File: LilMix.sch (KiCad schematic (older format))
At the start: 60 parts, among them J1_L1 MONO, J1_R1 MONO, J2_L1 MONO, J2_R1 MONO, J3 STEREO, J4 MONO, J5 MONO, J6 STEREO, U1 TL074, U2 NE5532

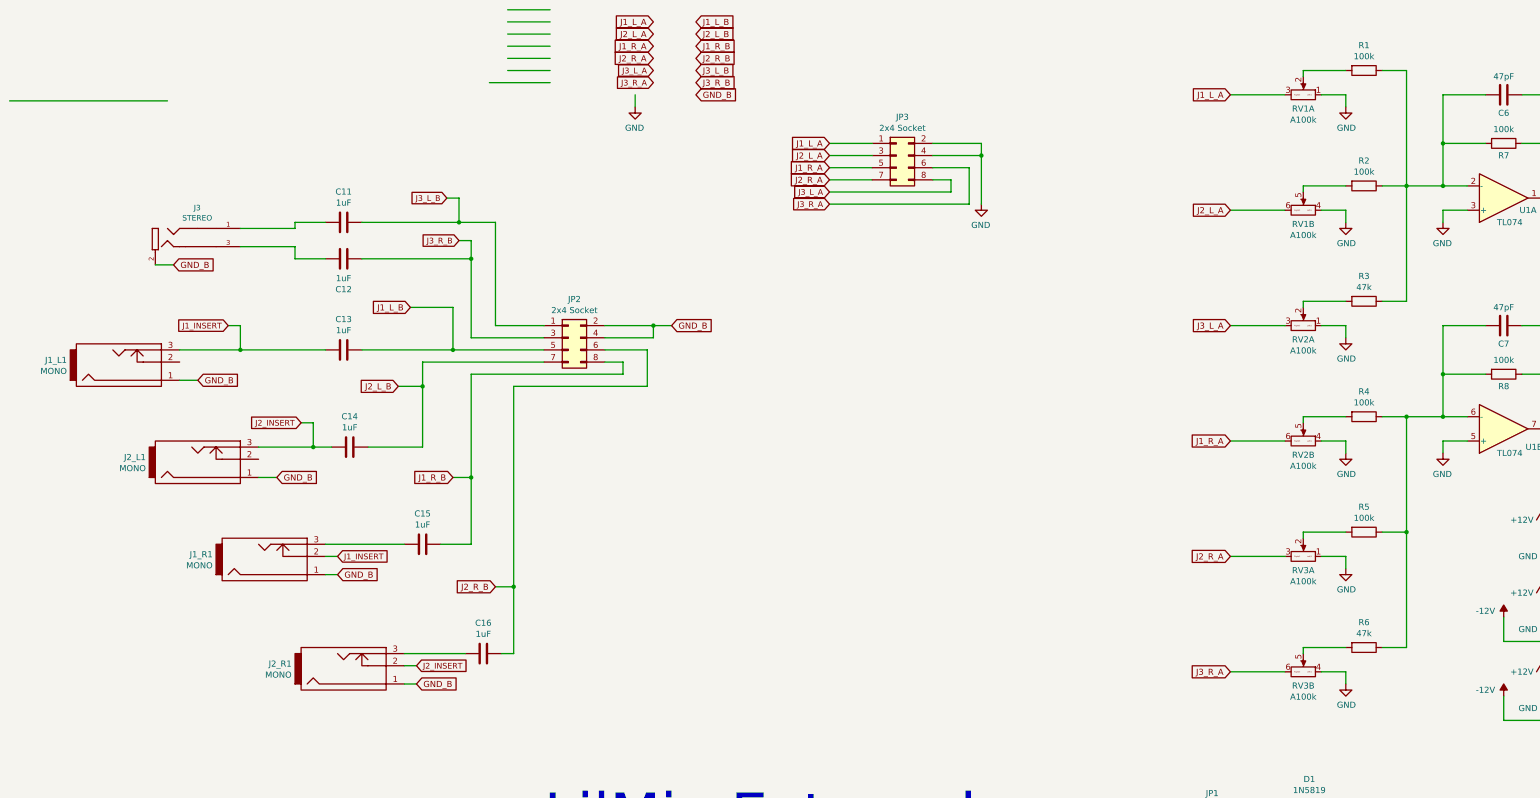
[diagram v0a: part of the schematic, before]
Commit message: Fixed jack destinatios and flipped front board orientation. Rerouted pcb
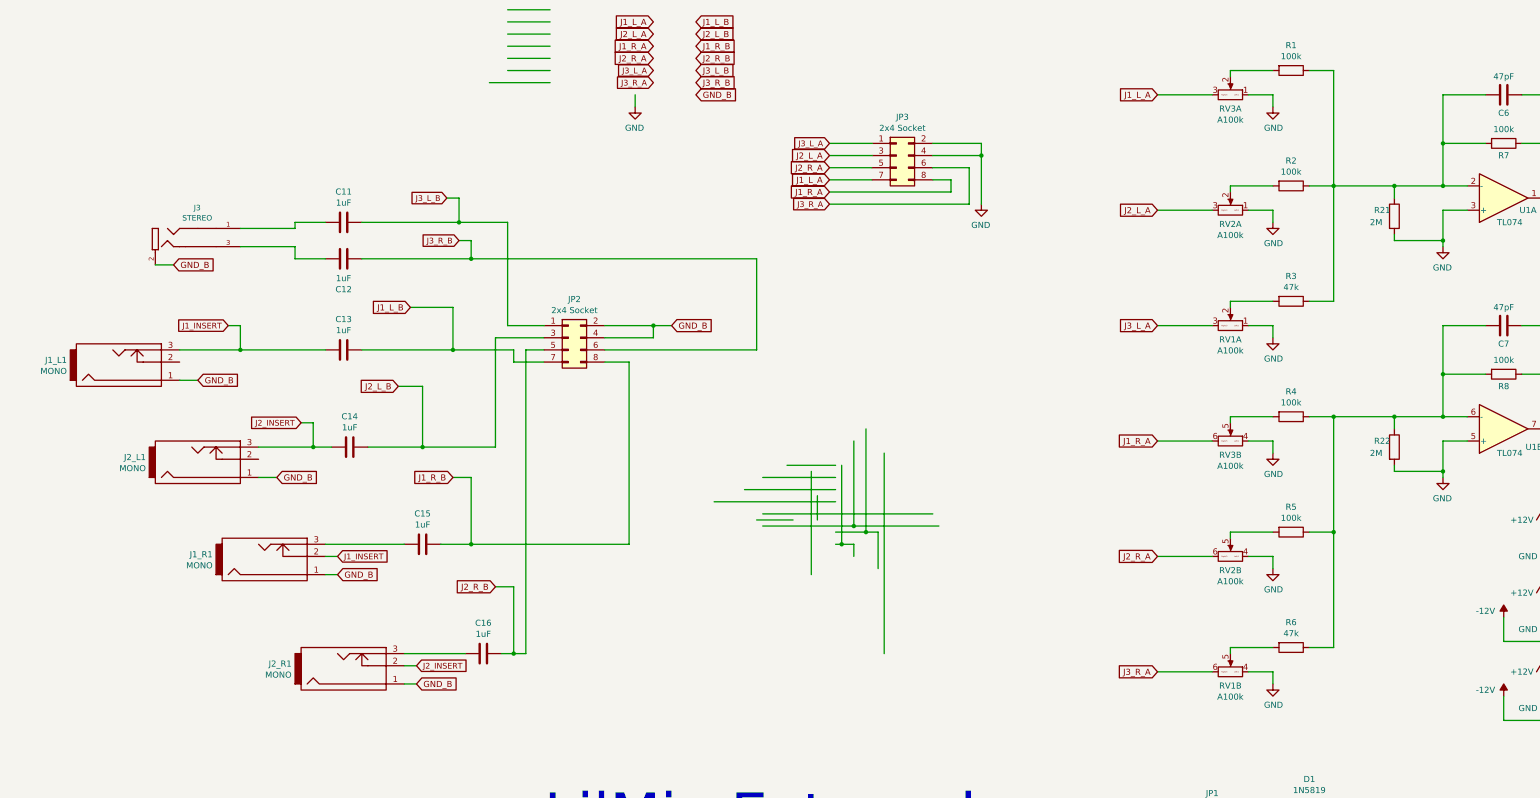
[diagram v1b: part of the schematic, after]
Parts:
- added R21, R22: 2M, Resistor_SMD:R_0805_2012Metric_Pad1.15x1.40mm_HandSolder, symbol 4ms-passives:R
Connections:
- wire segments 291 -> 322
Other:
- moved on the sheet: R1, R2, R3, R4, R5, R6, RV1A, RV1B, RV2A, RV2B, RV3A, RV3B

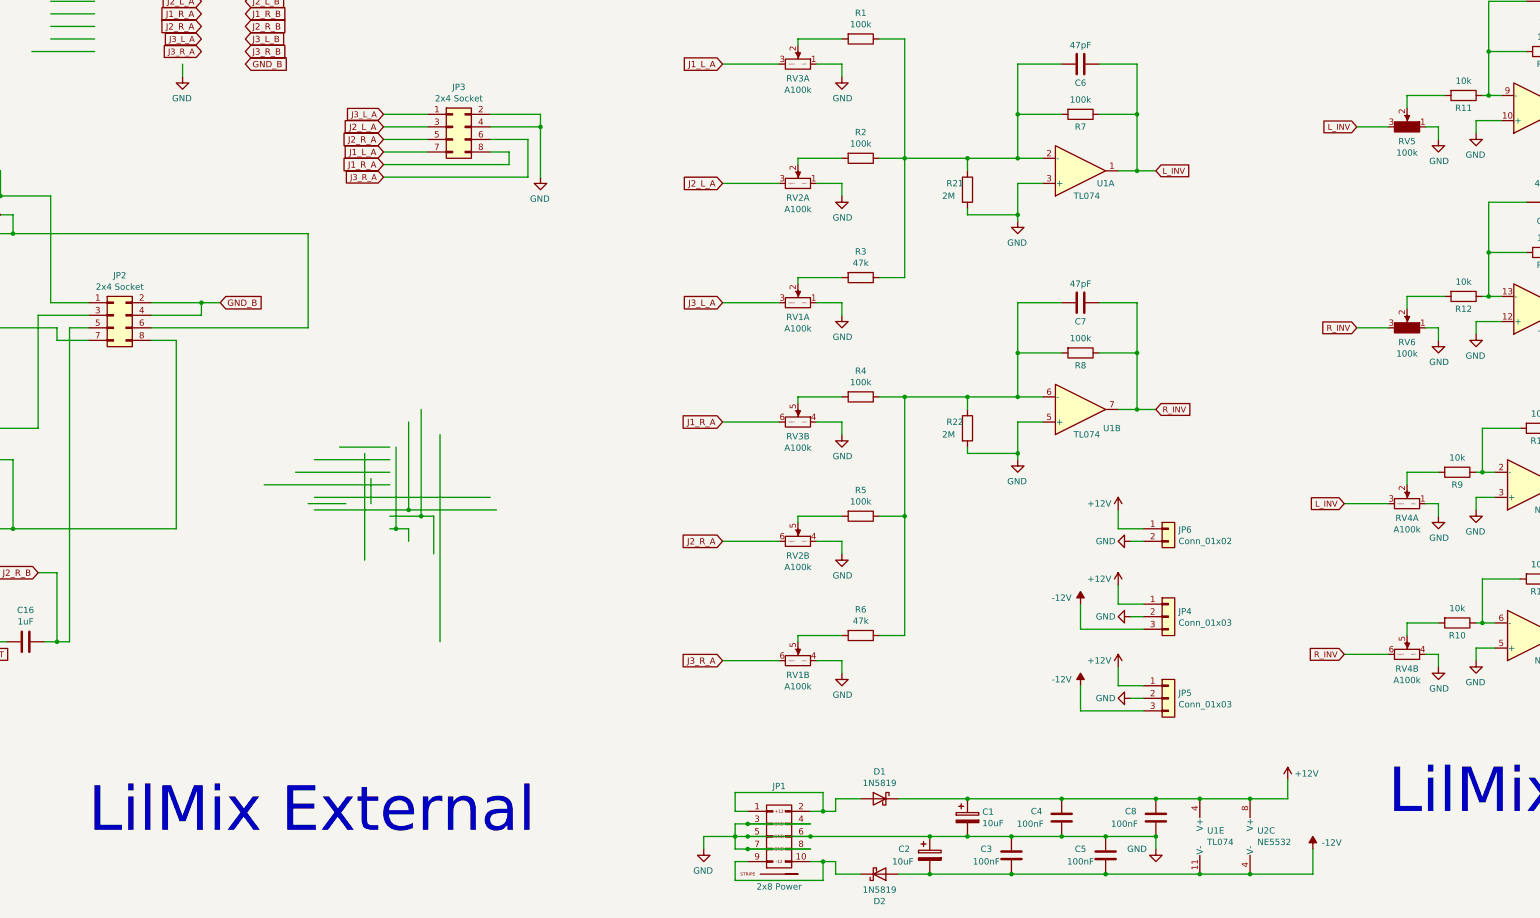
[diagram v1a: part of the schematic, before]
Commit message: Components moved, board wiring needs to be redone. Removed trim pots on line out. Replaced jacks on large board
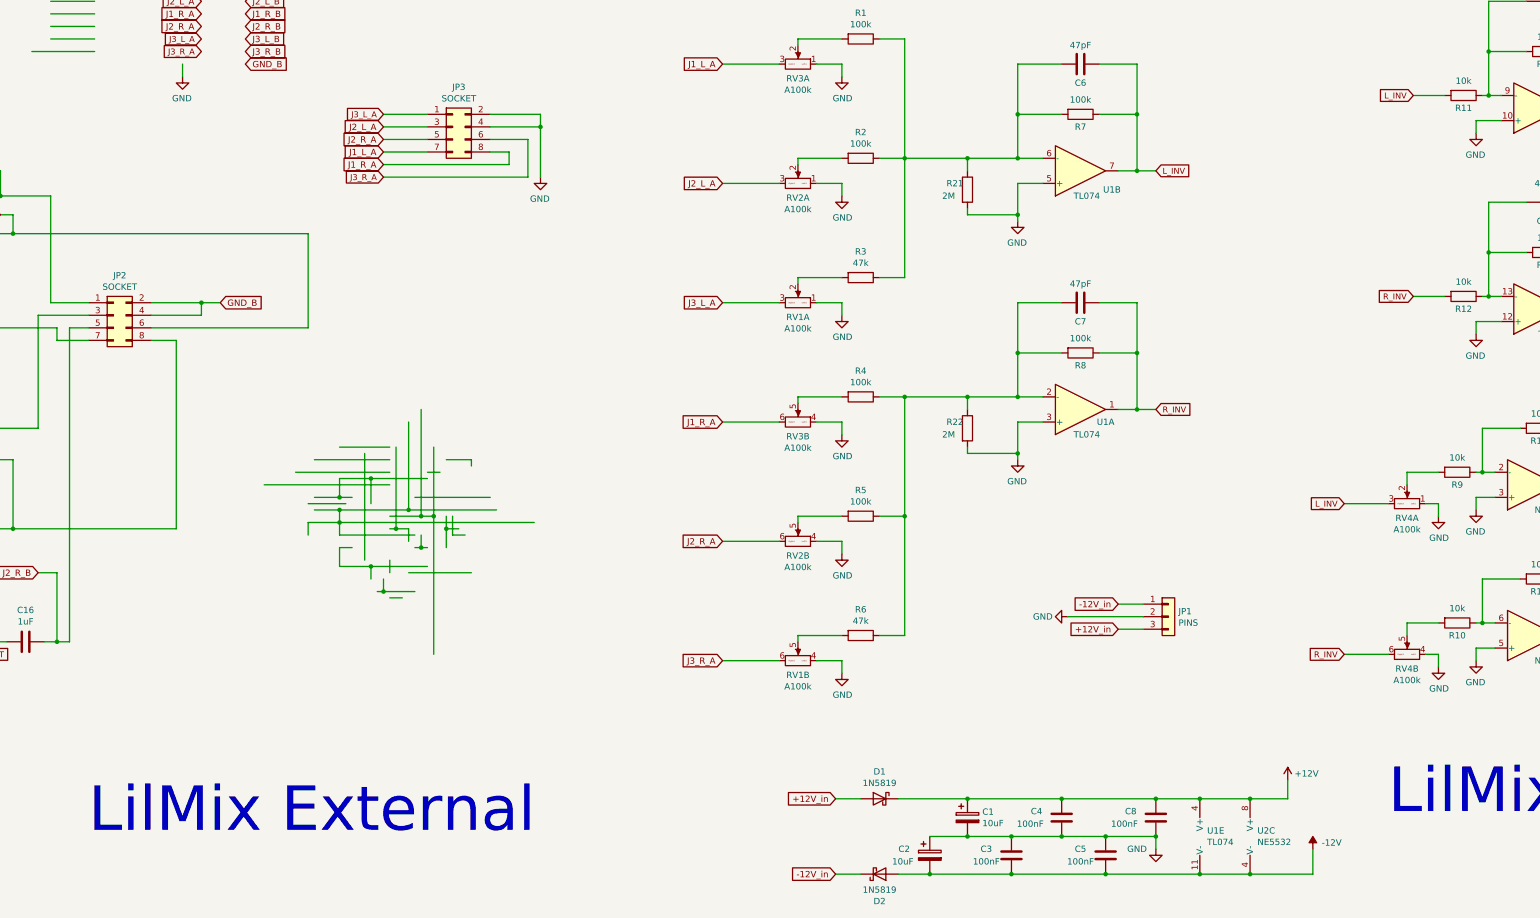
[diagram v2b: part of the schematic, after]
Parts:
- removed JP1: 2x8 Power, 4ms-footprints:Header_2x05_Pitch2.54mm_TH_-12v_Label, symbol 4ms-headers:EURO_HEADER_10pin
- removed JP5: Conn_01x03, Connector_PinSocket_2.54mm:PinSocket_1x03_P2.54mm_Vertical, symbol 4ms-headers:Conn_01x03
- removed JP6: Conn_01x02, Connector_PinSocket_2.54mm:PinSocket_1x02_P2.54mm_Vertical, symbol 4ms-headers:Conn_01x02
- removed RV5, RV6: 100k, 4ms-footprints:Audio_Mod_Header_1x03, symbol 4ms-mech:TRIMPOT
- J4, J5: footprint 4ms-footprints:PJ301M-12 -> Eurocad:EighthInch_PJ301BM_CC_FIXED
- JP1: renamed from JP4; value Conn_01x03 -> PINS
- JP2, JP3: value 2x4 Socket -> SOCKET
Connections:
- net labels added: +12V_in, -12V_in
- wire segments 322 -> 313
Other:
- moved on the sheet: U1A, U1B
